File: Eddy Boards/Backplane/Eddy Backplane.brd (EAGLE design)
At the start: 254 x 101.6 mm, 46 parts, among them J1 USB_MINI-B_SMT, P1 39-30-02?_S, P3 39-30-04?_S

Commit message: backplane update
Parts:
- moved J1 12.1 mm to (205.7, 94.0)
- moved R20 12.1 mm to (209.6, 88.3)
- moved R21 12.1 mm to (209.6, 85.7)
- moved R17 1.80 mm to (200.7, 71.8), turned to 90 degrees
- moved R18 1.80 mm to (200.7, 76.8), turned to 270 degrees
- moved C8 0.63 mm to (201.3, 80.6), turned to 180 degrees
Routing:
- net 3.3V: track 28.4 -> 296.3 mm, vias 5 -> 23
- net PLTA_ON/OFF: track 129.1 -> 290.2 mm, vias 2 -> 8
- net 5V: track 38.3 -> 173.1 mm, vias 8 -> 16
- net ROBOT_SDA: track 185.0 -> 306.1 mm, vias 0 -> 9
- net ROBOT_SCL: track 189.4 -> 307.5 mm, vias 0 -> 9
- net 3.3V_ON/OFF: track 129.1 -> 232.9 mm, vias 0 -> 4
- net 5V_ON/OFF: track 129.1 -> 228.4 mm, vias 0 -> 4
- net BACKPLANE_SDA: track 179.5 -> 278.5 mm, vias 0 -> 10
- net CONTROL_SIGNAL: track 129.1 -> 227.9 mm, vias 2 -> 4
- net BACKPLANE_SCL: track 184.2 -> 282.2 mm, vias 0 -> 10
- net 12V_ON/OFF: track 129.1 -> 224.1 mm, vias 0 -> 3
- net ACOUSTIC_ON/OFF: track 129.1 -> 219.7 mm, vias 0 -> 3
- net JETSON_ON/OFF: track 129.1 -> 215.4 mm, vias 0 -> 3
- net MOBO_ON/OFF: track 129.1 -> 211.2 mm, vias 0 -> 2
- net SPARE7: track 129.1 -> 207.5 mm
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- added copper zone on layer 16, net GND

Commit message: information about Copro needs
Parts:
- added C13, C14, C15, C16: (no value), rcl:C0603
- added D5: (no value), diode:SMB
- added P2: RB1-125BAG1A, RJ45-MAGJACK:WIZNET_RB1-125BAG1A
- added R19, R22, R23, R24: (no value), rcl:R0603
- added U1: W5500, W5500:QFP50P900X900X160-48N
- added Y1: (no value), SparkFun-Clocks:HC49US
- R20: value 5K -> 10k
- R21: value 10K -> 33k
- moved C12 45.5 mm to (231.1, 99.1), turned to 180 degrees
- moved 32.768KHZ 42.1 mm to (231.1, 97.2), turned to 180 degrees
- moved C11 38.9 mm to (231.1, 95.2), turned to 0 degrees
- moved R17 35.9 mm to (231.1, 90.8)
- moved C10 34.4 mm to (218.4, 99.1), turned to 180 degrees
- moved R18 32.9 mm to (231.8, 87.6), turned to 0 degrees
- moved 16MHZ 32.4 mm to (218.4, 97.2), turned to 180 degrees
- moved P1 32.4 mm to (236.9, 26.7)
- moved C9 30.5 mm to (218.4, 95.2), turned to 0 degrees
- moved C8 28.0 mm to (229.2, 81.9), turned to 0 degrees
- moved SWITCH_CONNECTOR 27.3 mm to (236.2, 59.1)
- moved C5 24.7 mm to (225.4, 89.5), turned to 270 degrees
- moved C7 22.8 mm to (226.7, 85.7), turned to 90 degrees
- moved C4 20.4 mm to (222.2, 89.5), turned to 270 degrees
- moved U$4 20.2 mm to (223.5, 88.3), turned to 180 degrees
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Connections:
- new net +3V3: U1.11, U1.15, U1.17, U1.21, U1.28, U1.4, U1.8
- new net N$10: C16.1, R22.2, U1.31, Y1.1
- new net N$11: R24.2, U1.25
- new net N$12: R23.2, U1.27
- new net N$13: C13.1, U1.20
- new net N$14: R19.2, U1.10
- new net N$15: P2.L1, R23.1
- new net N$16: P2.L3, R24.1
- new net N$4: C14.1, U1.22
- new net N$8: D5.C, R20.1
- new net N$9: C15.1, R22.1, U1.30, Y1.2
- new net NET_INTERRUPT: U1.36
- new net NET_RESET: U1.37
- new net SPI_CLK: U$4.21, U1.33
- new net SPI_MISO: U$4.22, U1.34
- new net SPI_MOSI: U$4.23, U1.35
- new net SPI_SS: U1.32
- net GND: now also C13.2, C14.2, C15.2, C16.2, P2.L2, P2.L4, R19.1, U1.14, U1.16, U1.19, U1.23, U1.29, U1.3, U1.48, U1.9
- net KILL_SWITCH: now also SWITCH_CONNECTOR.2; no longer SWITCH_CONNECTOR.4
- net SWITCH_2: now also SWITCH_CONNECTOR.4; no longer SWITCH_CONNECTOR.2
- net VBUS: now also D5.A; no longer R20.1
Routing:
- net 3.3V: track 296.3 -> 62.4 mm, vias 23 -> 8
- net PLTA_ON/OFF: track 290.2 -> 129.1 mm, vias 8 -> 0
- net 5V: track 173.1 -> 59.2 mm, vias 16 -> 8
- net SWITCH_2: track 259.8 -> 147.8 mm
- net SWITCH_1: track 260.4 -> 155.4 mm, vias 1 -> 0
- net SWITCH_3: track 257.7 -> 156.7 mm
- net CONTROL_SIGNAL: track 227.9 -> 129.1 mm, vias 4 -> 0
- net ROBOT_SCL: track 307.5 -> 211.3 mm, vias 9 -> 0
- net SWITCH_4: track 246.9 -> 150.9 mm, vias 6 -> 0
- net ROBOT_SDA: track 306.1 -> 212.7 mm, vias 9 -> 0
- net KILL_SWITCH: track 260.0 -> 167.4 mm, vias 2 -> 0
- net BACKPLANE_SDA: track 278.5 -> 202.5 mm, vias 10 -> 0
- net BACKPLANE_SCL: track 282.2 -> 207.6 mm, vias 10 -> 0
- net 12V_ON/OFF: track 224.1 -> 183.3 mm, vias 3 -> 0
- net ACOUSTIC_ON/OFF: track 219.7 -> 181.4 mm, vias 3 -> 0
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- added copper zone on layer 1, net 3.3V
- added copper zone on layer 1, net 5V
- added copper zone on layer 16, net ISOLATION
- removed copper zone on layer 16, net 3.3V
- removed copper zone on layer 16, net 5V
- removed copper zone on layer 1, net GND

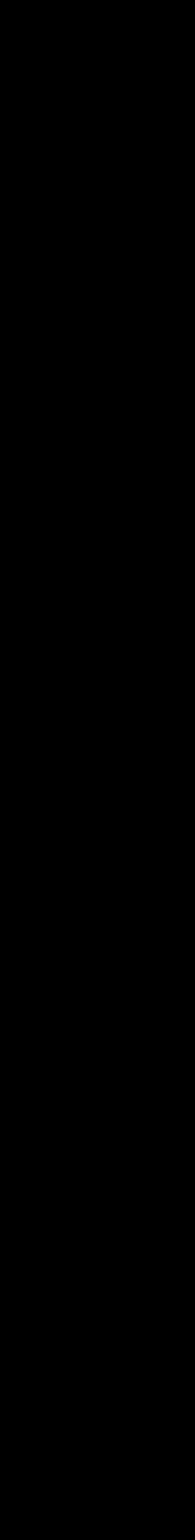
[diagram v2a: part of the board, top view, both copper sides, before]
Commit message: Updated Copro PWM drivers and programming header
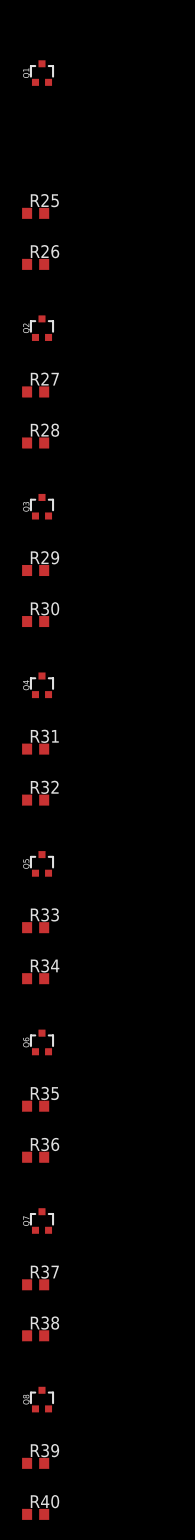
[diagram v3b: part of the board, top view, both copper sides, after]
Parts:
- added Q1, Q2, Q3, Q4, Q5, Q6, Q7, Q8: 310mA/60V/1.6Ω, SparkFun-DiscreteSemi:SOT323
- added R25, R26, R27, R28, R29, R30, R31, R32, R33, R34, R35, R36, R37, R38, R39, R40: 10k, rcl:R0603
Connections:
- new net N$17: Q2.2, R27.2
- new net N$19: Q1.2, R25.2
- new net N$21: Q3.2, R29.2
- new net N$23: Q4.2, R31.2
- new net N$25: Q5.2, R33.2
- new net N$27: Q6.2, R35.2
- new net N$29: Q7.2, R37.2
- new net N$31: Q8.2, R39.2
- net 3.3V: now also Q1.1, Q2.1, Q3.1, Q4.1, Q5.1, Q6.1, Q7.1, Q8.1, R25.1, R27.1, R29.1, R31.1, R33.1, R35.1, R37.1, R39.1
- net 5V: now also R26.1, R28.1, R30.1, R32.1, R34.1, R36.1, R38.1, R40.1
- net PWM_1: now also Q1.3, R26.2
- net PWM_2: now also Q5.3, R34.2
- net PWM_3: now also Q2.3, R28.2
- net PWM_4: now also Q6.3, R36.2
- net PWM_5: now also Q3.3, R30.2
- net PWM_6: now also Q7.3, R38.2
- net PWM_7: now also Q4.3, R32.2
- net PWM_8: now also Q8.3, R40.2
